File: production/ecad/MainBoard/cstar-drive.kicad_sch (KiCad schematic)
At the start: 55 parts, among them J1 B4B-PH-K-S, J2 B4B-PH-K-S, J3 Conn_01x03_Pin, J4 Conn_01x03_Pin, J5 Conn_01x03_Pin, J6 Conn_01x03_Pin, J7 Conn_01x03_Pin, J8 Conn_01x03_Pin, J9 Conn_01x03_Pin, U1 DRV8842PWPR, U2 DRV8842PWPR, X1 B2P-VH, X2 B2P-VH

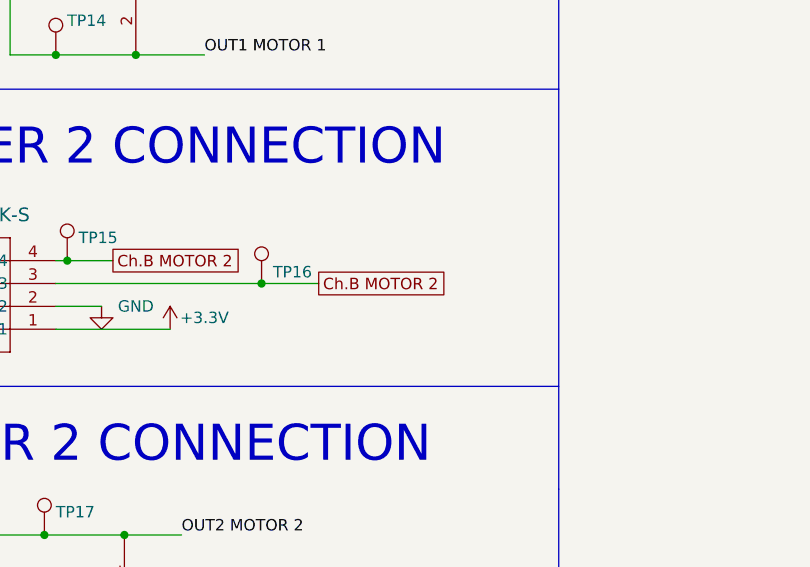
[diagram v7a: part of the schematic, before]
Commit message: "Misspelled Global Net Fix"
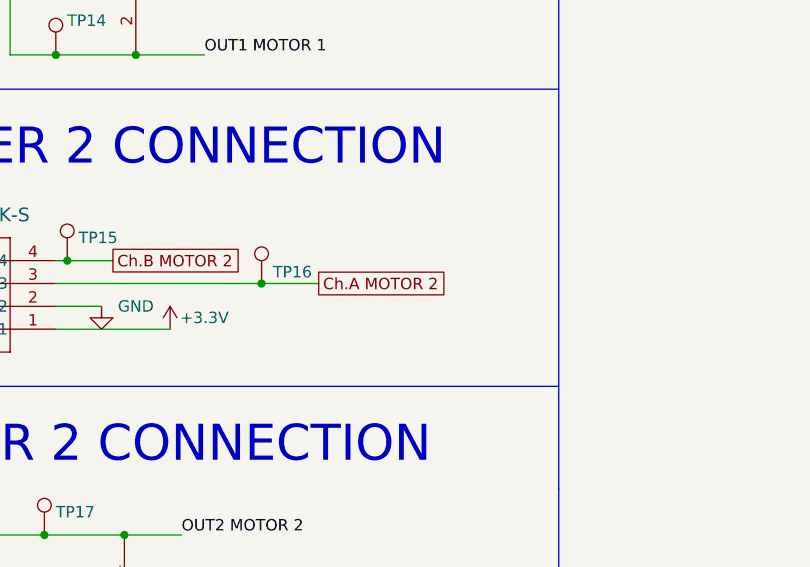
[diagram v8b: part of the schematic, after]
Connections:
- net Ch.B MOTOR 2: no longer J2.3, TP16.1
- new net Ch.A MOTOR 2: J2.3, TP16.1
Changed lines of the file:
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@@
     )
   )
-  (global_label "Ch.B MOTOR 2" (shape passive) (at 255.27 130.81 0) (fields_autoplaced)
+  (global_label "Ch.A MOTOR 2" (shape passive) (at 255.27 130.81 0) (fields_autoplaced)
     (effects (font (size 1.27 1.27)) (justify left))
-    (property "Intersheetrefs" "${INTERSHEET_REFS}" (at 270.9324 130.81 0)
+    (property "Intersheetrefs" "${INTERSHEET_REFS}" (at 270.751 130.81 0)
       (effects (font (size 1.27 1.27)) (justify left) hide)
     )
